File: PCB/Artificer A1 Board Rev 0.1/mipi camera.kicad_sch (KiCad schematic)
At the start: 4 parts

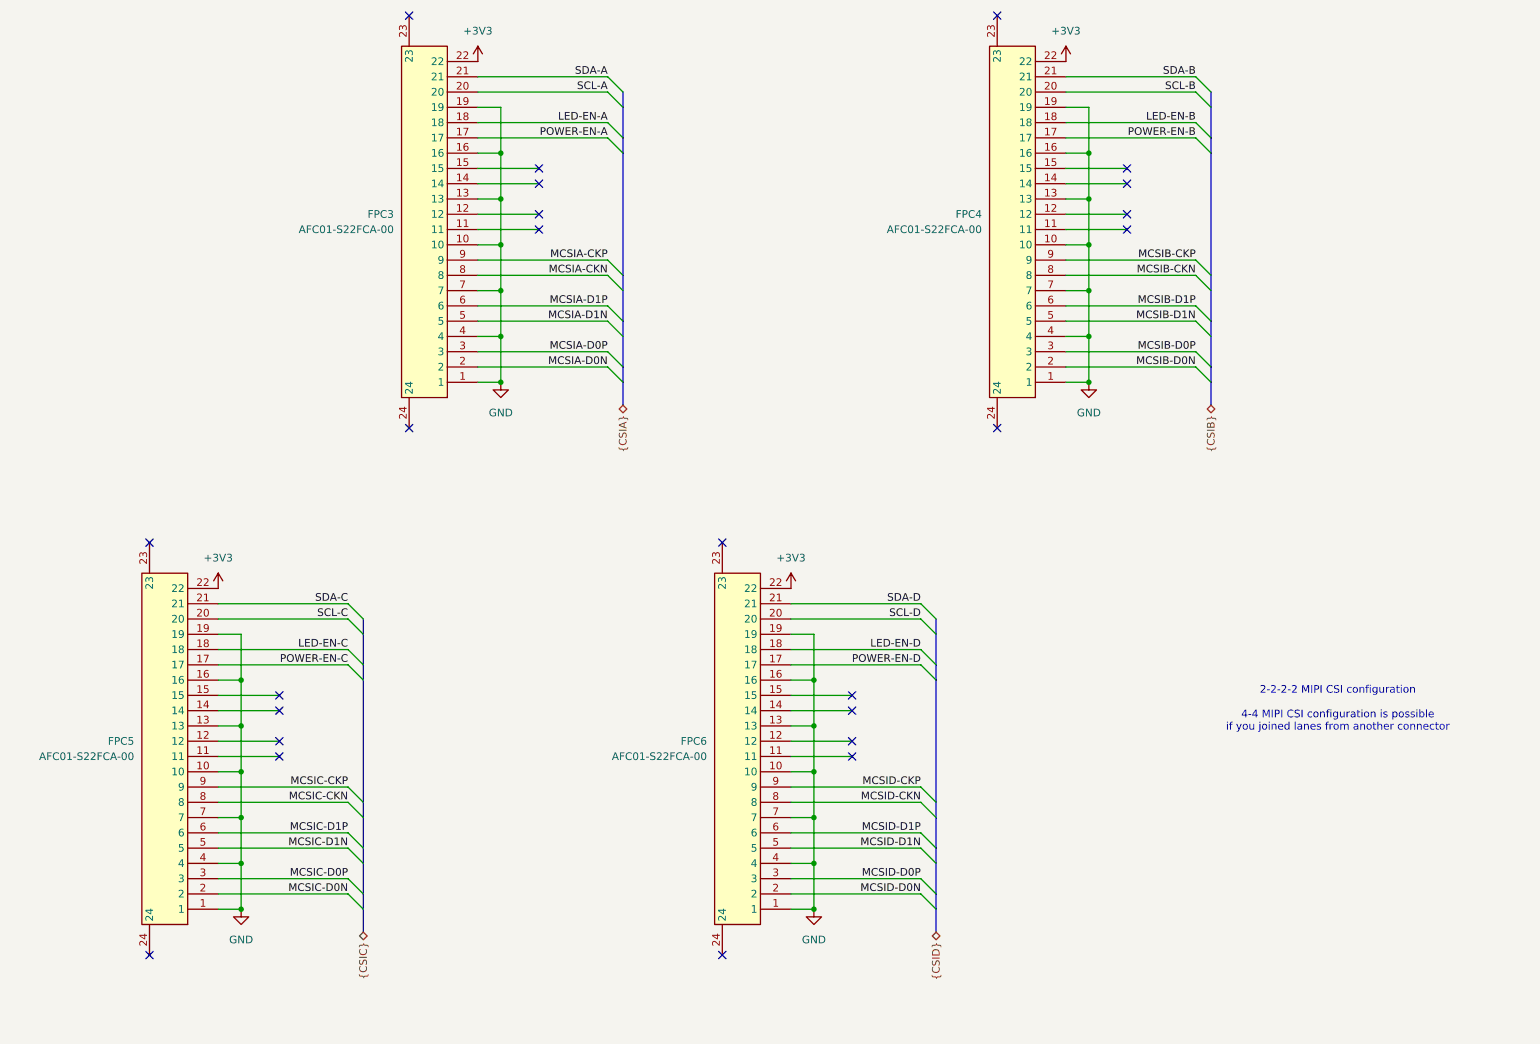
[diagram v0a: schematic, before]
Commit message: added HDMI, DP, DSI, etc
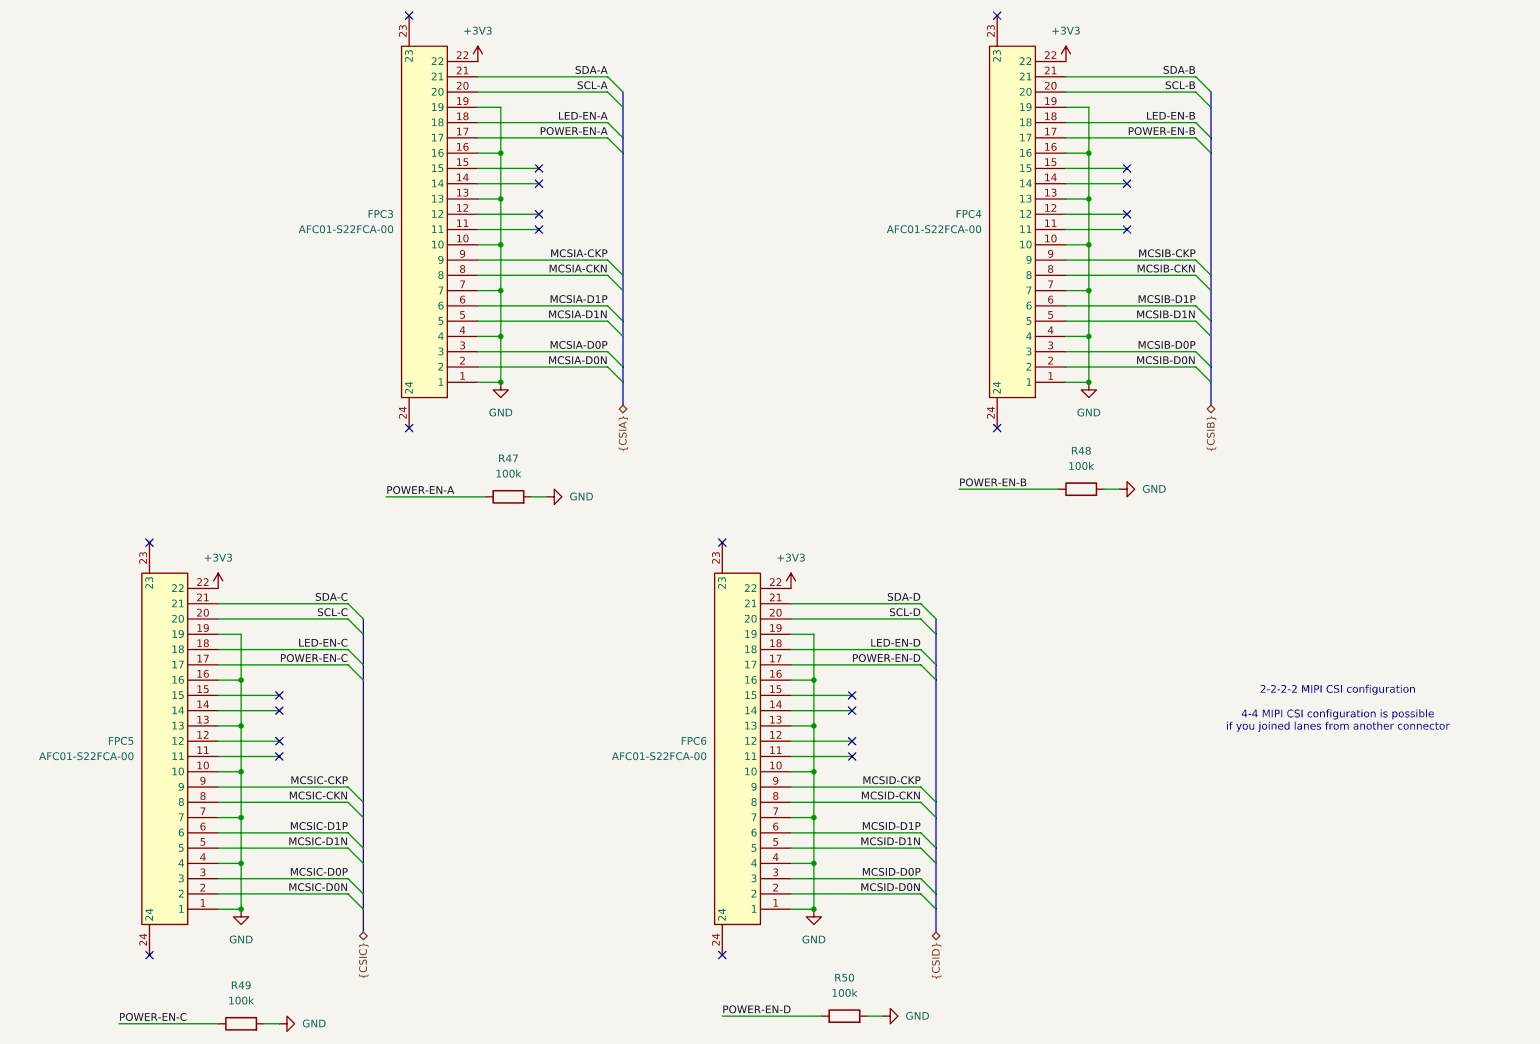
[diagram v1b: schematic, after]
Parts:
- added R47, R48, R49, R50: 100k, symbol Device:R
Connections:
- net GND: now also R47.2, R48.2, R49.2, R50.2
- net POWER-EN-A: now also R47.1
- net POWER-EN-B: now also R48.1
- net POWER-EN-C: now also R49.1
- net POWER-EN-D: now also R50.1

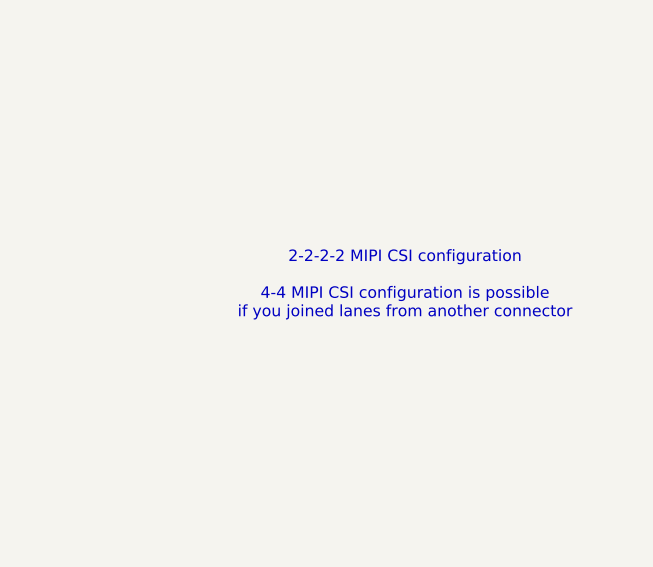
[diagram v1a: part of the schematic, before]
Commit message: finished dram
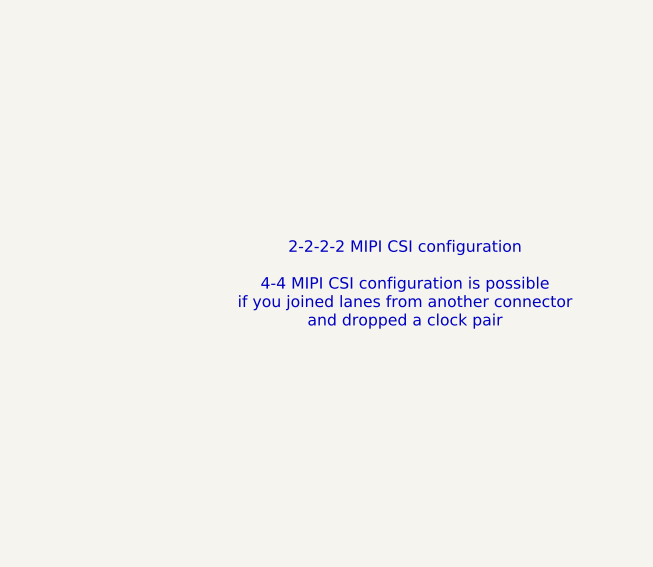
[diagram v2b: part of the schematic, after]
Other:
- note added: "2-2-2-2 MIPI CSI configuration 4-4 MIPI CSI configuration is possible if you joined lanes from another connector and dropped a clock pair"
- note removed: "2-2-2-2 MIPI CSI configuration 4-4 MIPI CSI configuration is possible if you joined lanes from another connector"
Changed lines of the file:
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@@
 		)
 	)
-	(text "2-2-2-2 MIPI CSI configuration\n\n4-4 MIPI CSI configuration is possible\nif you joined lanes from another connector\n"
+	(text "2-2-2-2 MIPI CSI configuration\n\n4-4 MIPI CSI configuration is possible\nif you joined lanes from another connector\nand dropped a clock pair"
 		(exclude_from_sim no)
 		(at 235.712 140.716 0)

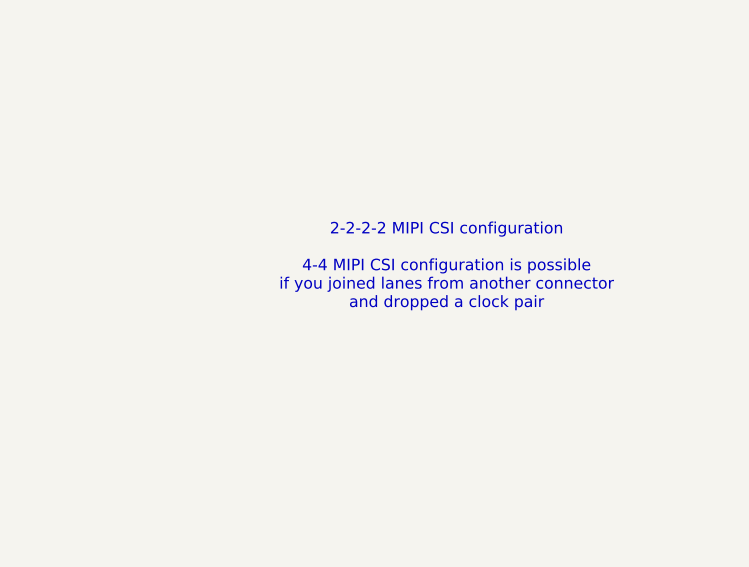
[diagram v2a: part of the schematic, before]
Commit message: added: sd, wifi, audio, started power, fixed buses
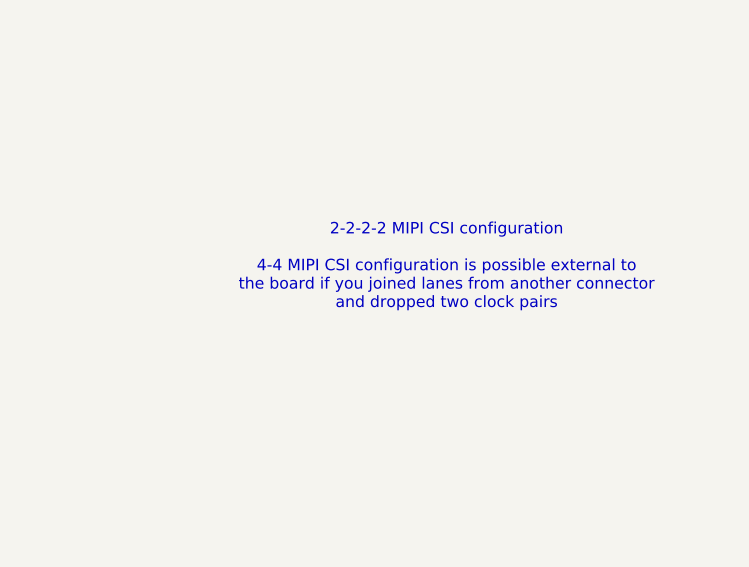
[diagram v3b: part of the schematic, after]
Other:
- note added: "2-2-2-2 MIPI CSI configuration 4-4 MIPI CSI configuration is possible external to the board if you joined lanes from another connector and dropped two clock pairs"
- note removed: "2-2-2-2 MIPI CSI configuration 4-4 MIPI CSI configuration is possible if you joined lanes from another connector and dropped a clock pair"
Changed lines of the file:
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@@
 		)
 	)
-	(text "2-2-2-2 MIPI CSI configuration\n\n4-4 MIPI CSI configuration is possible\nif you joined lanes from another connector\nand dropped a clock pair"
+	(text "2-2-2-2 MIPI CSI configuration\n\n4-4 MIPI CSI configuration is possible external to \nthe board if you joined lanes from another connector\nand dropped two clock pairs"
 		(exclude_from_sim no)
 		(at 235.712 140.716 0)
